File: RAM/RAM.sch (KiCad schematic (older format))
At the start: 19 parts, among them J1 Conn_01x16, J2 Conn_01x16, J3 Conn_01x16, J4 Conn_01x16, U1 HM62256BLP, U2 74LS02, U3 74LS245

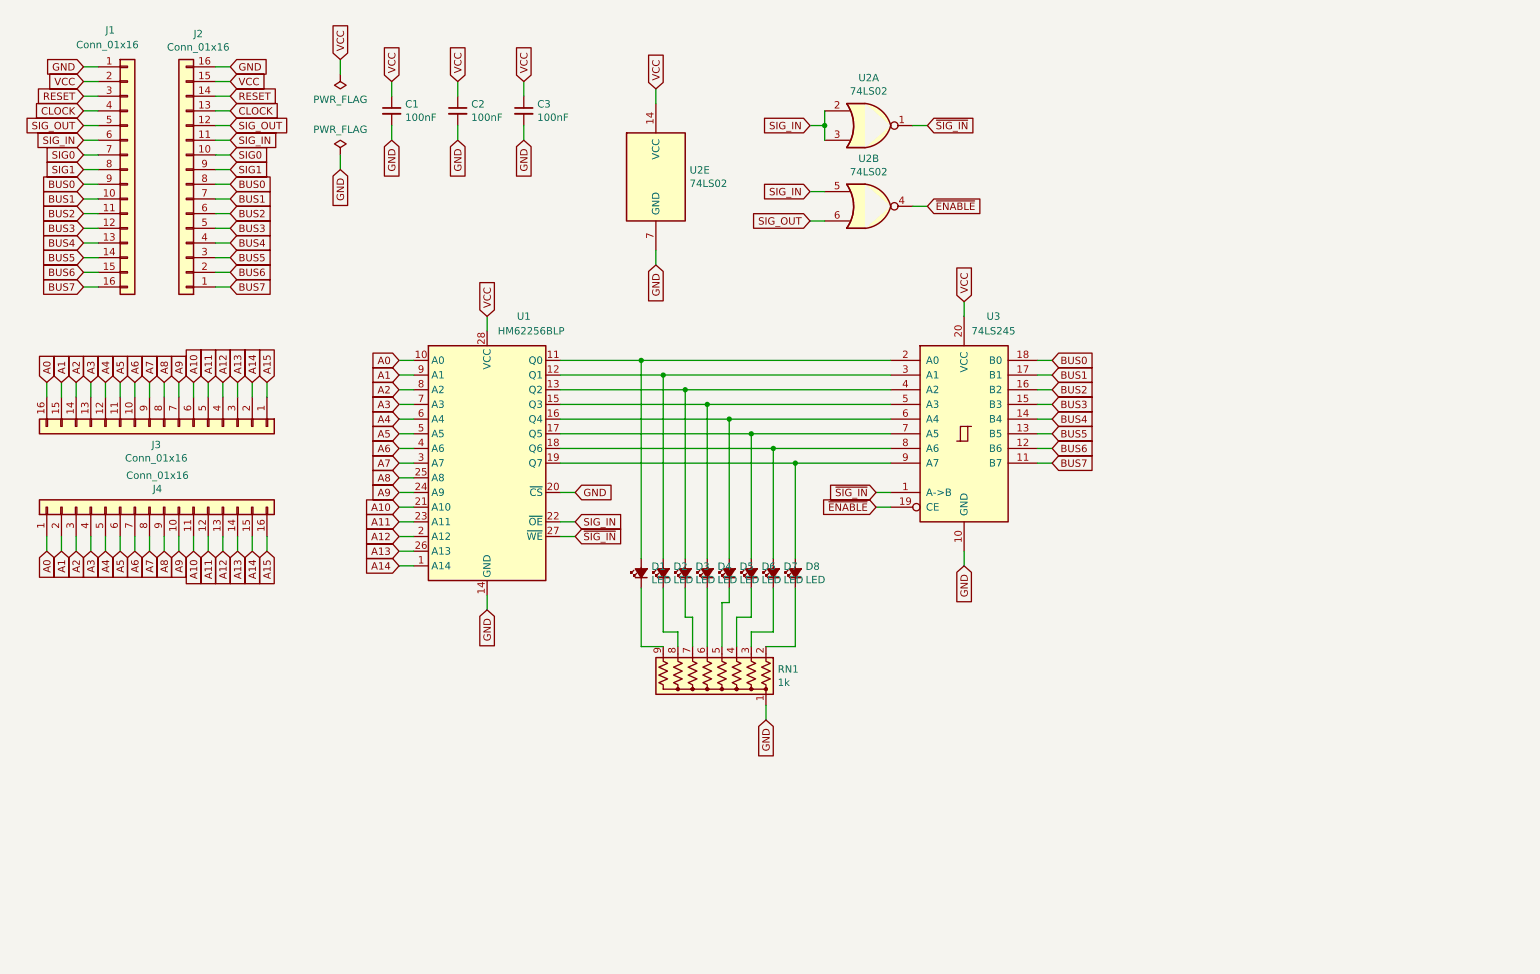
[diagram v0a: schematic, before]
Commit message: Fixed floating inputs; improved power; added parts list; replaced JK latches
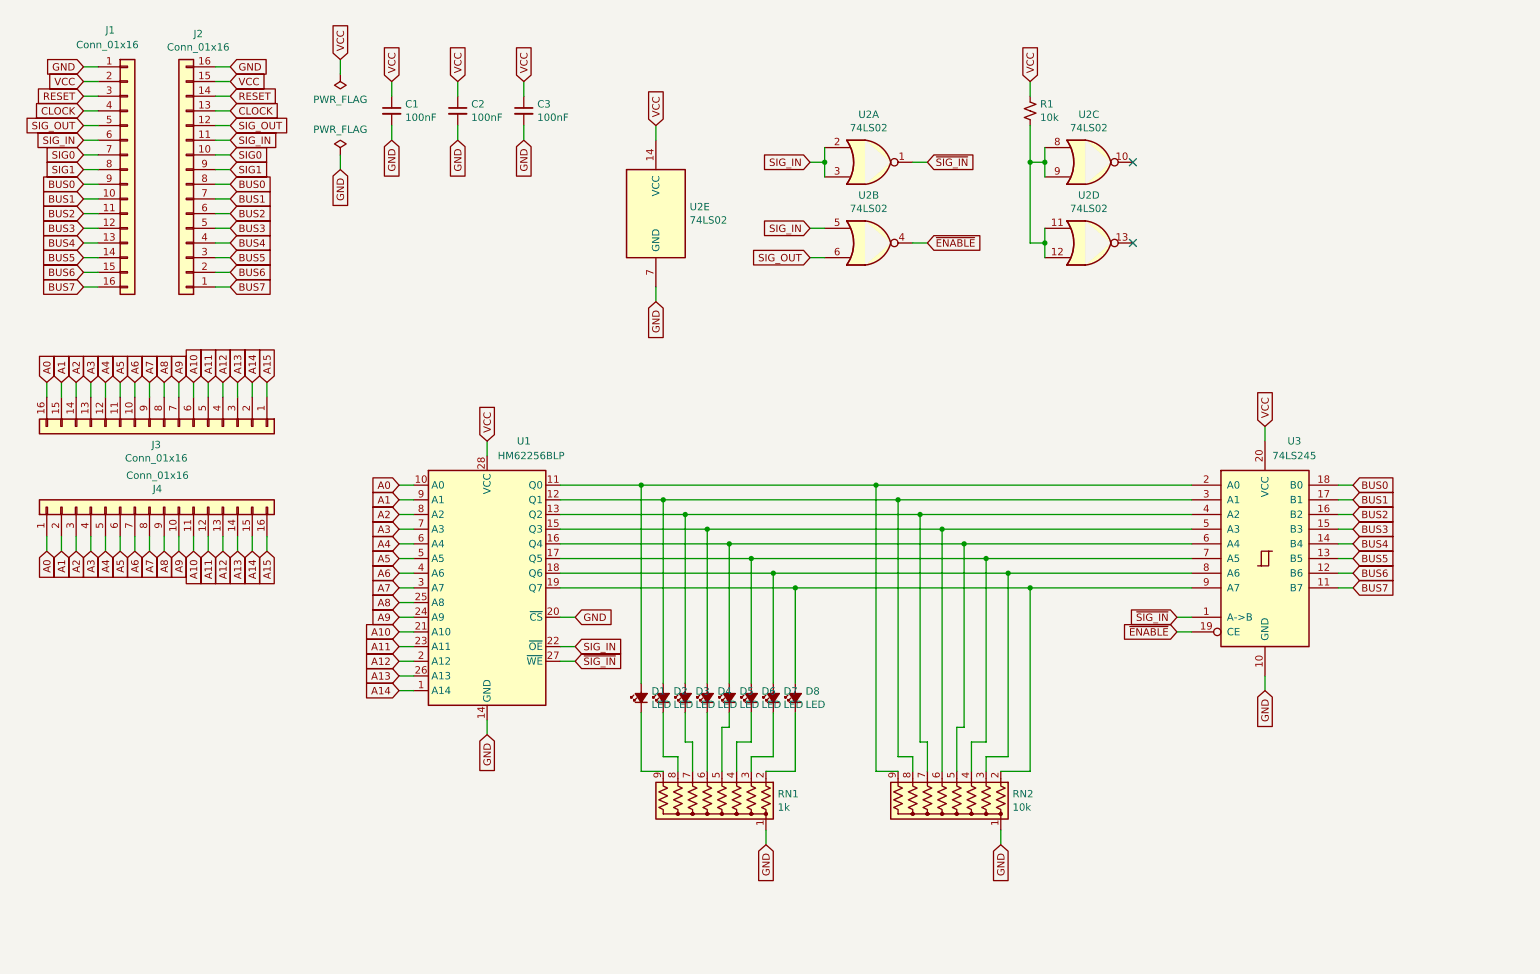
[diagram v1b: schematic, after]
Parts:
- added R1: 10k, Resistor_THT:R_Axial_DIN0207_L6.3mm_D2.5mm_P7.62mm_Horizontal, symbol Device:R_Small_US
- added RN2: 10k, Resistor_THT:R_Array_SIP9, symbol Device:R_Network08_US
- added unit 3 of U2
- added unit 4 of U2
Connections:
- net GND: now also RN2.1 (common)
- net VCC: now also R1.1
- net at D1.2 (A), U1.11 (Q0), U3.2 (A0): now also RN2.9 (R8)
- net at D2.2 (A), U1.12 (Q1), U3.3 (A1): now also RN2.8 (R7)
- net at D3.2 (A), U1.13 (Q2), U3.4 (A2): now also RN2.7 (R6)
- net at D4.2 (A), U1.15 (Q3), U3.5 (A3): now also RN2.6 (R5)
- net at D5.2 (A), U1.16 (Q4), U3.6 (A4): now also RN2.5 (R4)
- net at D6.2 (A), U1.17 (Q5), U3.7 (A5): now also RN2.4 (R3)
- net at D7.2 (A), U1.18 (Q6), U3.8 (A6): now also RN2.3 (R2)
- net at D8.2 (A), U1.19 (Q7), U3.9 (A7): now also RN2.2 (R1)
- new net: R1.2, U2.11, U2.12, U2.8, U2.9
- no-connect marks 0 -> 2
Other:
- moved on the sheet: D1, D2, D3, D4, D5, D6, D7, D8, RN1, U1, U2A, U2B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

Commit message: Revise control and RAM modules
- Change control signals on low going clock
- Pull down control signals with 1k resistors
- AND the write signal with clock on RAM / ROM module
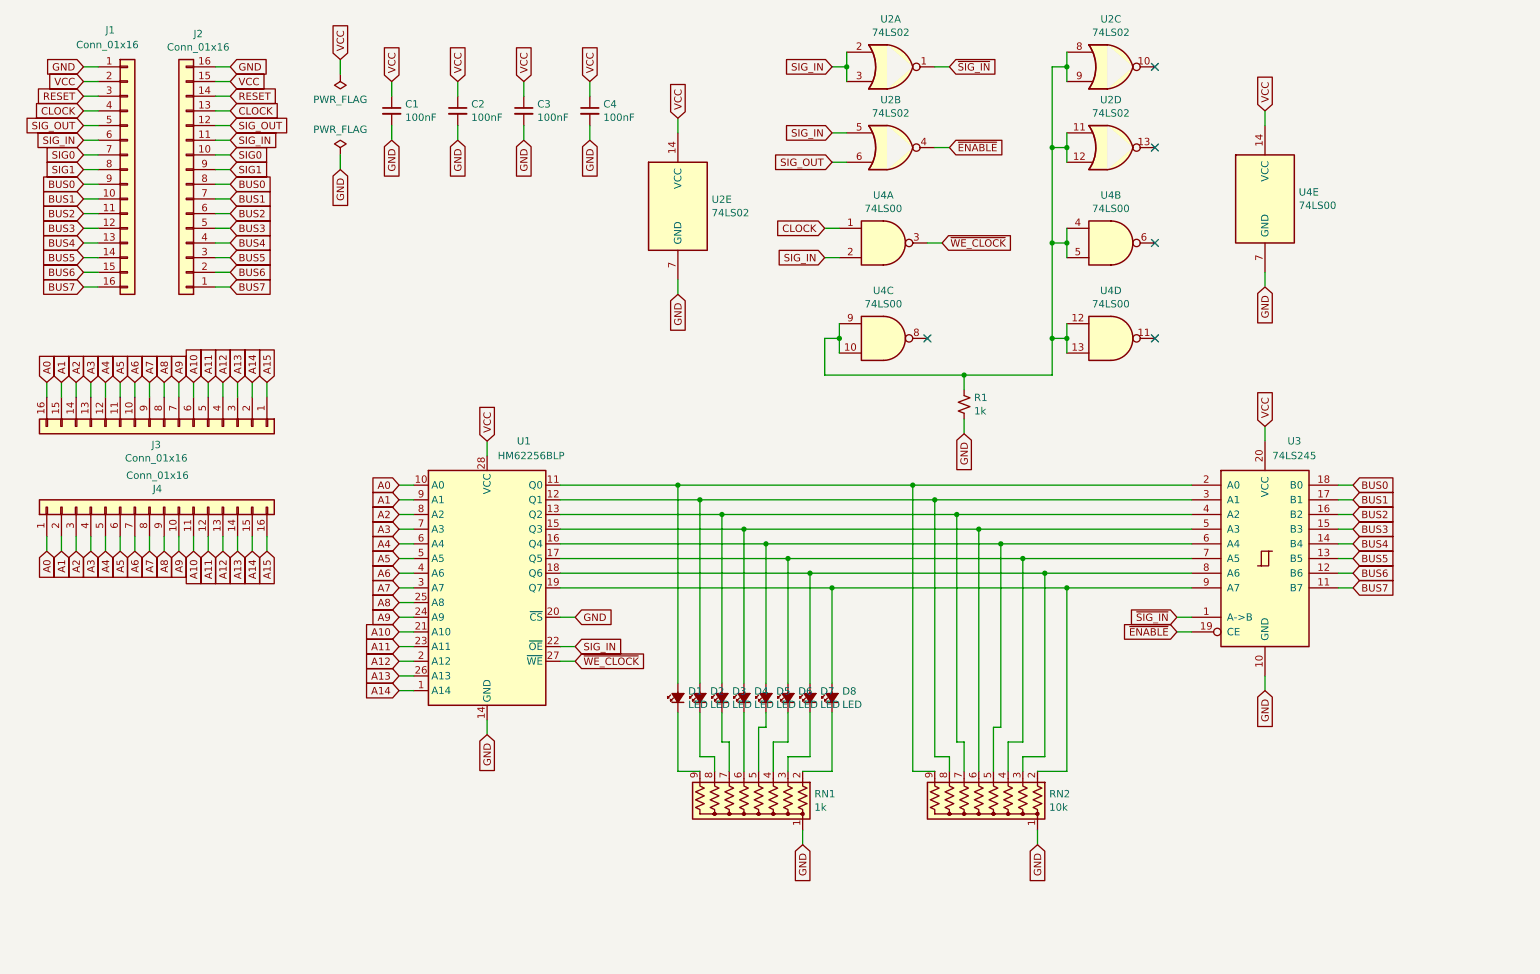
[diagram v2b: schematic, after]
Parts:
- added C4: 100nF, Capacitor_THT:C_Disc_D4.3mm_W1.9mm_P5.00mm, symbol Device:C_Small
- added U4: 74LS00, Package_DIP:DIP-14_W7.62mm, symbol 74xx:74LS00
- R1: value 10k -> 1k
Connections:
- net CLOCK: now also U4.1
- net GND: now also R1.2, C4.2, U4.7 (GND)
- net SIG_IN: now also U4.2
- net VCC: now also C4.1, U4.14 (VCC); no longer R1.1
- net ~SIG_IN: no longer U1.27 (~WE)
- net at U2.11, U2.12, U2.8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: now also R1.1, U4.10, U4.12, U4.13, U4.4, U4.5, U4.9; no longer R1.2
- new net ~WE_CLOCK: U1.27 (~WE), U4.3
- no-connect marks 2 -> 5
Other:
- moved on the sheet: D1, D2, D3, D4, D5, D6, D7, D8, RN1, RN2, U2A, U2B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

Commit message: Update all boards to r3, and update revision log and gitignore
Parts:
- removed R1: 1k, Resistor_THT:R_Axial_DIN0207_L6.3mm_D2.5mm_P7.62mm_Horizontal, symbol Device:R_Small_US
- added J5: 3183-10200P1T, updated_libs:318310200P1T, symbol 3183-10200P1T:3183-10200P1T
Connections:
- net A0: now also J5.A4
- net A1: now also J5.A5
- net A10: now also J5.B6
- net A11: now also J5.B7
- net A12: now also J5.B8
- net A13: now also J5.B9
- net A14: now also J5.B10
- net A15: now also U1.20 (~CS), U4.10, U4.9
- net A2: now also J5.A6
- net A3: now also J5.A7
- net A4: now also J5.A8
- net A5: now also J5.A9
- net A6: now also J5.A10
- net A7: now also J5.A11
- net A8: now also J5.B4
- net A9: now also J5.B5
- net GND: now also U2.11, U2.12, U2.8, U2.9, U4.12, U4.13, U4.4, U4.5, J5.A18, J5.A3, J5.B18, J5.B3; no longer U1.20 (~CS)
- net SIG_IN: now also J5.B11
- net VCC: now also J5.A12, J5.A2, J5.B1, J5.B12, J5.B2
- net ~WE_CLOCK: now also J5.A17
- net at RN2.9 (R8), U1.11 (Q0), U3.2 (A0): now also D8.2 (A), J5.A13; no longer D1.2 (A)
- net at RN2.8 (R7), U1.12 (Q1), U3.3 (A1): now also D7.2 (A), J5.A14; no longer D2.2 (A)
- net at RN2.7 (R6), U1.13 (Q2), U3.4 (A2): now also D6.2 (A), J5.A15; no longer D3.2 (A)
- net at RN2.6 (R5), U1.15 (Q3), U3.5 (A3): now also D5.2 (A), J5.A16; no longer D4.2 (A)
- net at RN2.5 (R4), U1.16 (Q4), U3.6 (A4): now also D4.2 (A), J5.B13; no longer D5.2 (A)
- net at RN2.4 (R3), U1.17 (Q5), U3.7 (A5): now also D3.2 (A), J5.B14; no longer D6.2 (A)
- net at RN2.3 (R2), U1.18 (Q6), U3.8 (A6): now also D2.2 (A), J5.B15; no longer D7.2 (A)
- net at RN2.2 (R1), U1.19 (Q7), U3.9 (A7): now also D1.2 (A), J5.B16; no longer D8.2 (A)
- net ~CART_CS: now reaches U4.8
- net ~CART_CS: now also J5.A1, J5.B17
- no-connect marks 5 -> 4
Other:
- moved on the sheet: C1, C2, C3, C4, D1, D2, D3, D4, D5, D6, D7, D8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
